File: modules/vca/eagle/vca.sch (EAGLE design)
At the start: 73 parts, among them IC1 TL074P, IC2 LM13600AN, Q1 2N3906, Q2 2N3906, T1 2N3904, T2 2N3904

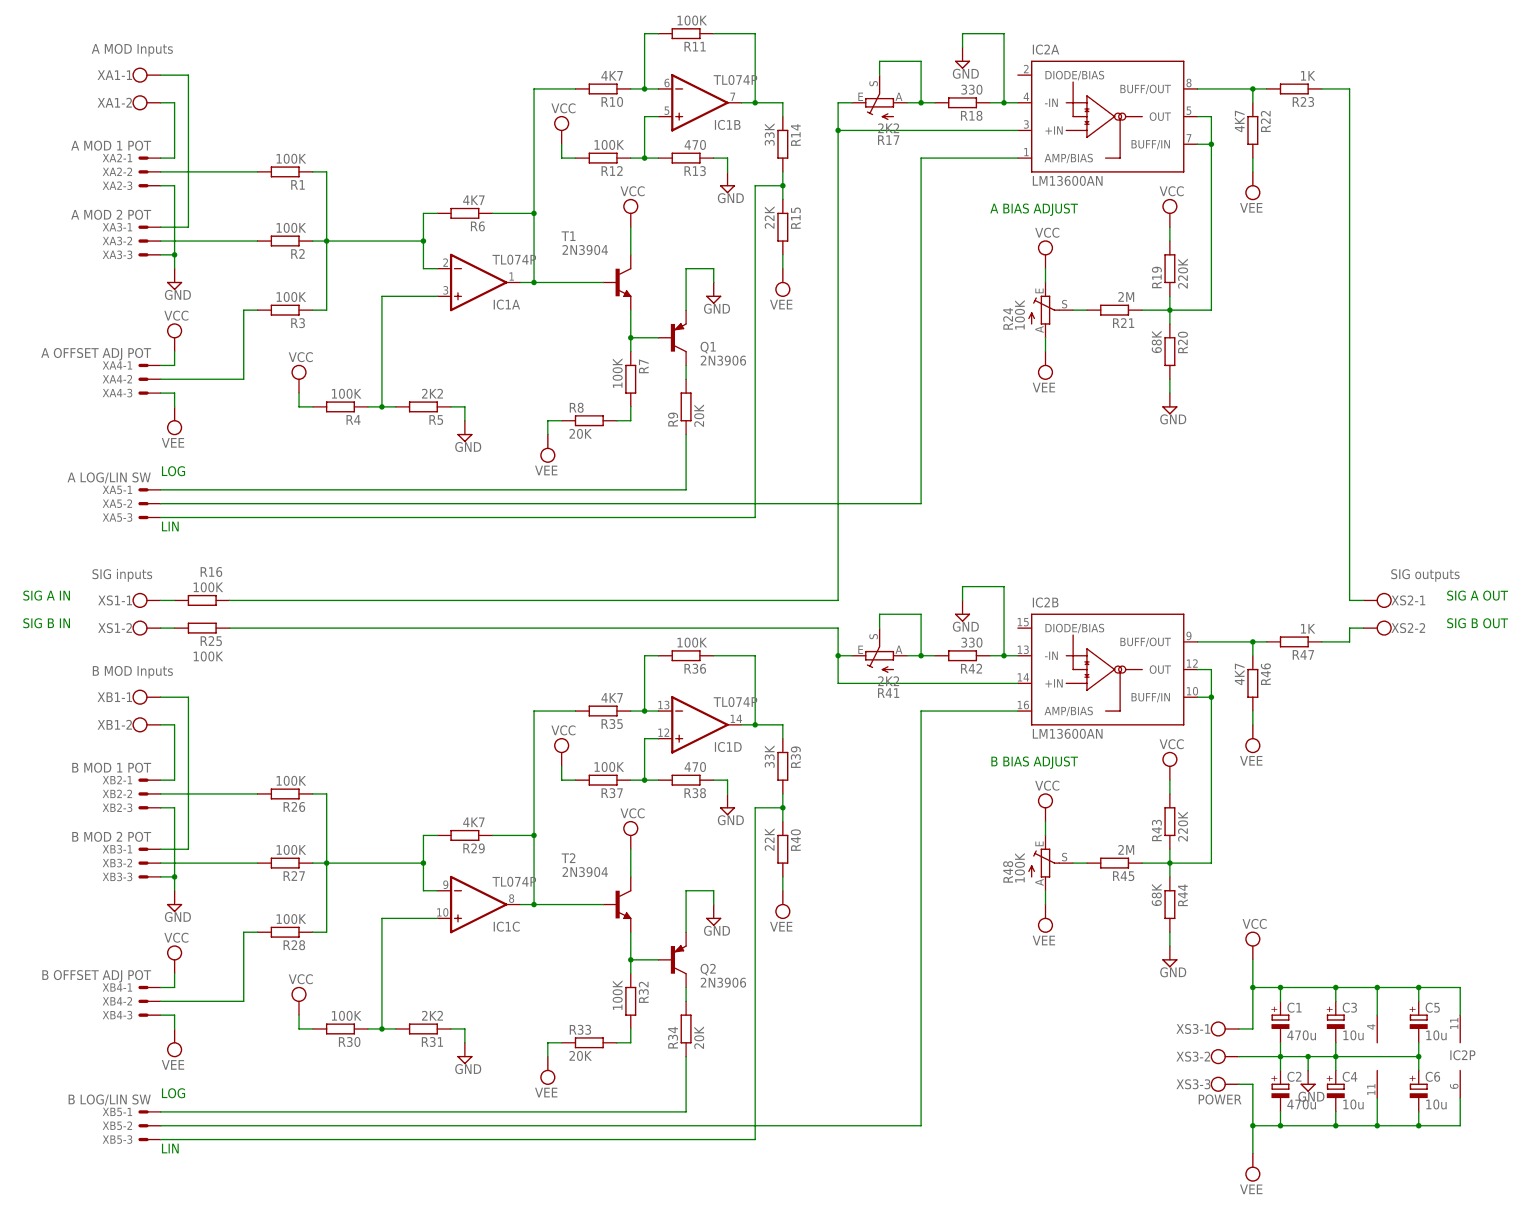
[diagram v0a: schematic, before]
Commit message: Basic layout of VCA board, still needs power
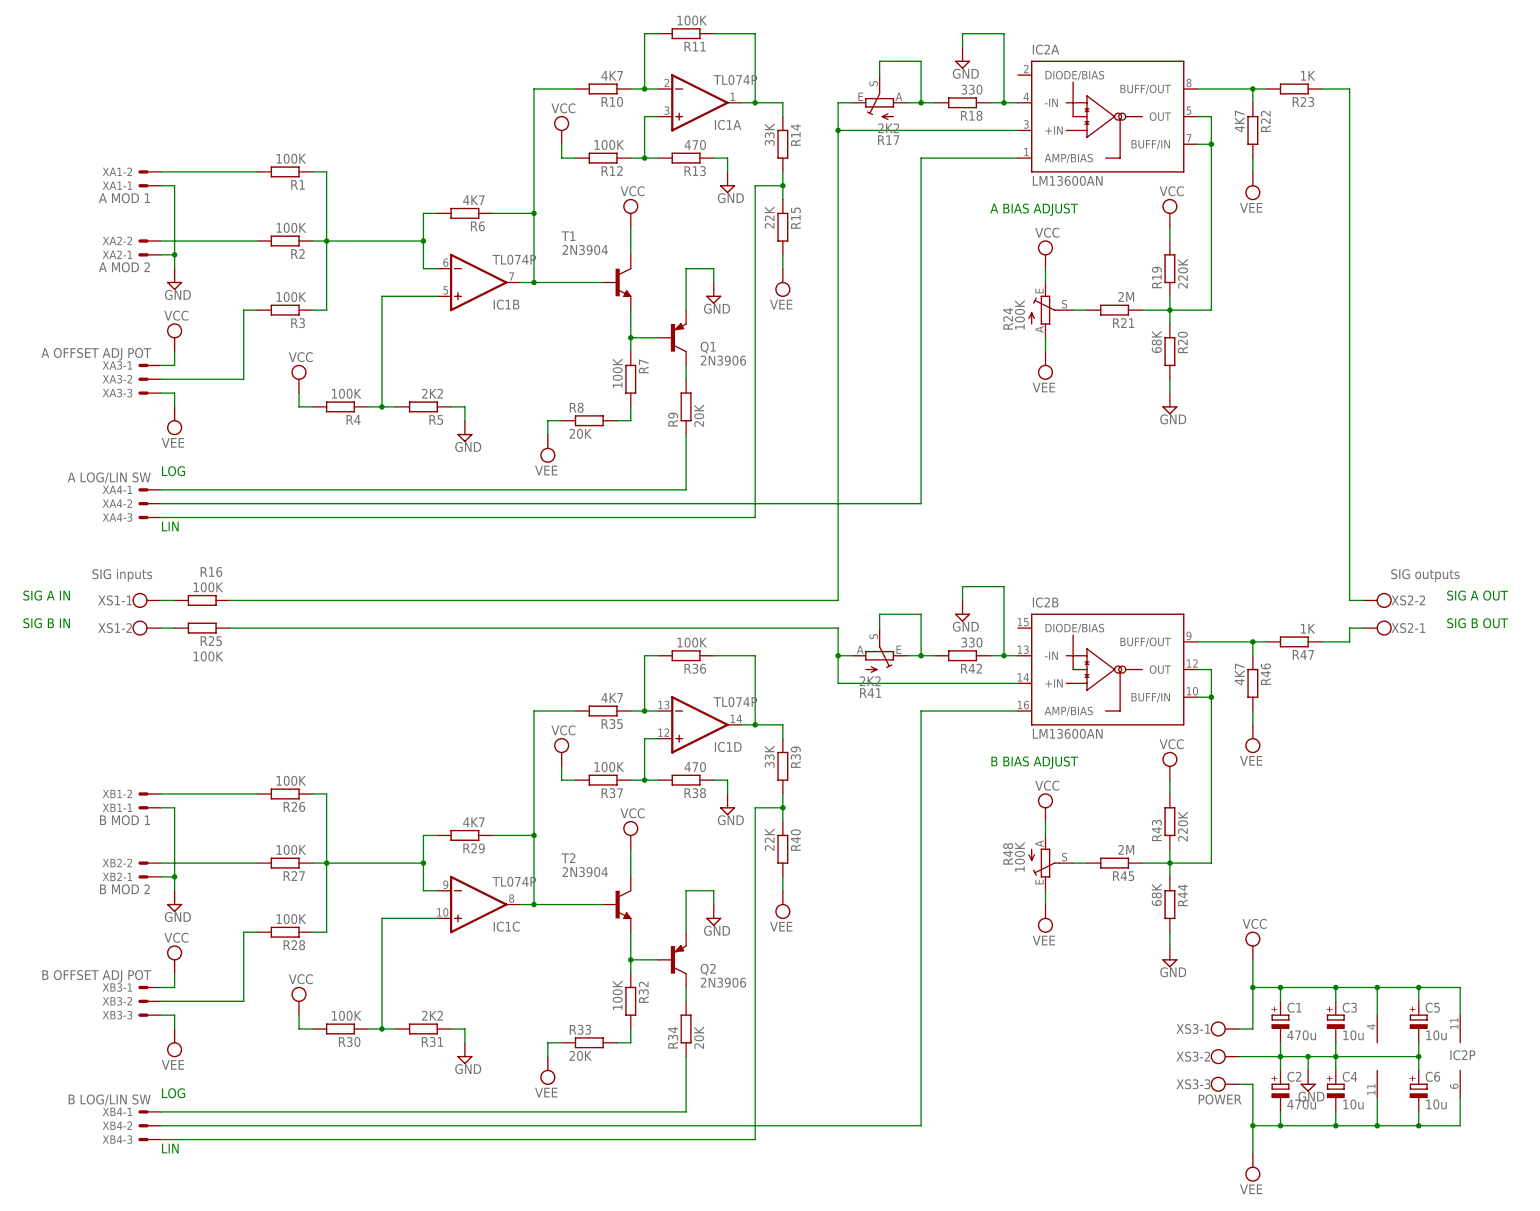
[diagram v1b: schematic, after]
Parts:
- removed XA5: A LOG/LIN SW, con-molex:22-23-2031
- removed XB5: B LOG/LIN SW, con-molex:22-23-2031
- XA1: value A MOD Inputs -> A MOD 1; device con-wago-500:W237-102 -> con-molex:22-23-2021
- XA2: value A MOD 1 POT -> A MOD 2; device con-molex:22-23-2031 -> con-molex:22-23-2021
- XA3: value A MOD 2 POT -> A OFFSET ADJ POT
- XA4: value A OFFSET ADJ POT -> A LOG/LIN SW
- XB1: value B MOD Inputs -> B MOD 1; device con-wago-500:W237-102 -> con-molex:22-23-2021
- XB2: value B MOD 1 POT -> B MOD 2; device con-molex:22-23-2031 -> con-molex:22-23-2021
- XB3: value B MOD 2 POT -> B OFFSET ADJ POT
- XB4: value B OFFSET ADJ POT -> B LOG/LIN SW
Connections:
- removed net N$19: XA1-1.KL, XA3-1.S
- removed net N$22: XA1-2.KL, XA2-1.S
- removed net N$33: XB1-2.KL, XB2-1.S
- removed net N$34: XB1-1.KL, XB3-1.S
- net GND: now also XA1-1.S, XA2-1.S, XB1-1.S, XB2-1.S; no longer XA2-3.S, XA3-3.S, XB2-3.S, XB3-3.S
- net N$1: now also IC1B.-IN; no longer IC1A.-IN
- net N$10: now also XA4-1.S; no longer XA5-1.S
- net N$11: now also IC1A.-IN; no longer IC1B.-IN
- net N$12: now also XA4-2.S; no longer XA5-2.S
- net N$13: now also IC1A.OUT; no longer IC1B.OUT
- net N$15: now also IC1A.+IN; no longer IC1B.+IN
- net N$17: now also XA4-3.S; no longer XA5-3.S
- net N$2: now also XA1-2.S; no longer XA2-2.S
- net N$25: now also R41.A; no longer R41.E
- net N$26: now also XB1-2.S; no longer XB2-2.S
- net N$27: now also XS2-2.KL; no longer XS2-1.KL
- net N$28: now also XB2-2.S; no longer XB3-2.S
- net N$29: now also XB3-2.S; no longer XB4-2.S
- net N$3: now also XA2-2.S; no longer XA3-2.S
- net N$30: now also XB4-1.S; no longer XB5-1.S
- net N$31: now also XS2-1.KL; no longer XS2-2.KL
- net N$32: now also XB4-2.S; no longer XB5-2.S
- net N$4: now also XA3-2.S; no longer XA4-2.S
- net N$45: now also XB4-3.S; no longer XB5-3.S
- net N$46: now also R41.E; no longer R41.A
- net N$5: now also IC1B.+IN; no longer IC1A.+IN
- net N$7: now also IC1B.OUT; no longer IC1A.OUT
- net VCC: now also R48.A, XA3-1.S, XB3-1.S; no longer R48.E, XA4-1.S, XB4-1.S
- net VEE: now also R48.E, XA3-3.S, XB3-3.S; no longer R48.A, XA4-3.S, XB4-3.S
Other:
- moved on the sheet: IC1A, IC1B, R48, XA1-1, XA1-2, XA2-1, XA2-2, XA3-1, XA3-2, XA3-3, XA4-1, XA4-2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

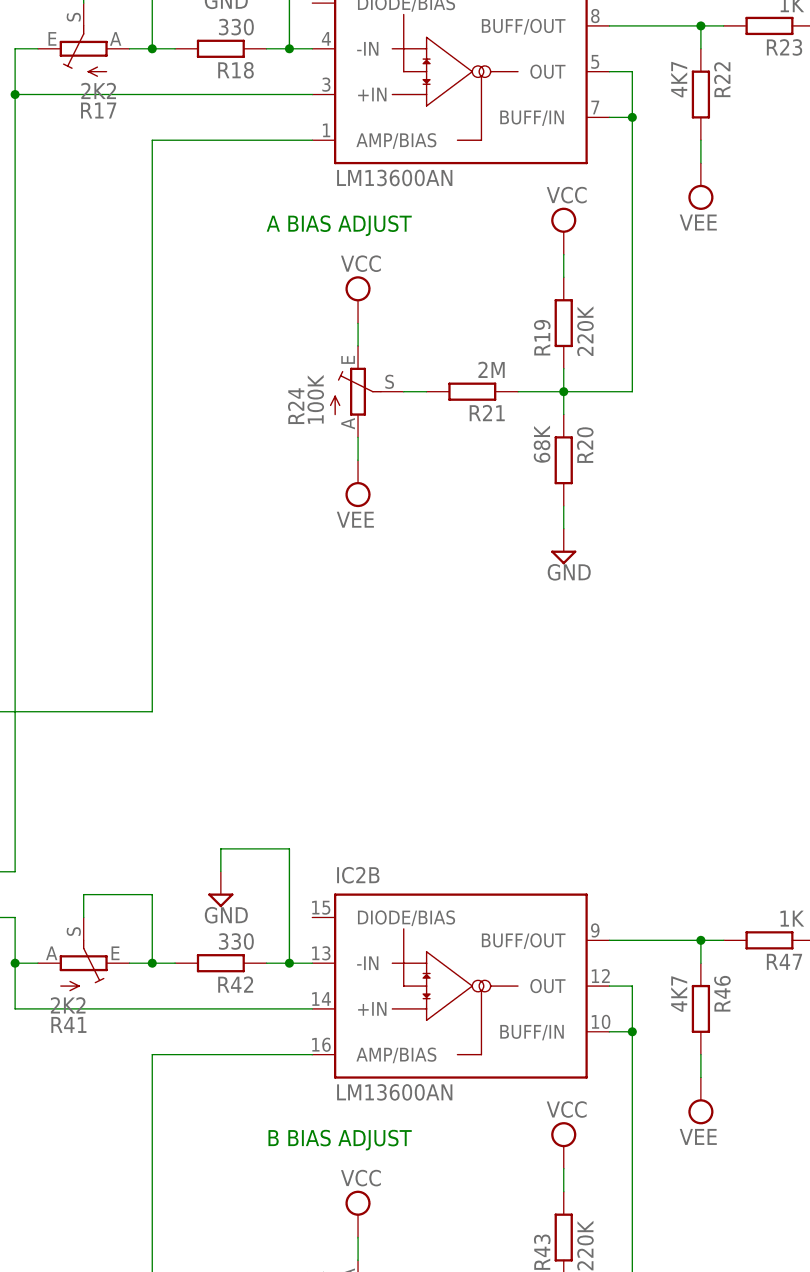
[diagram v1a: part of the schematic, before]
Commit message: Finish dual VCA board design
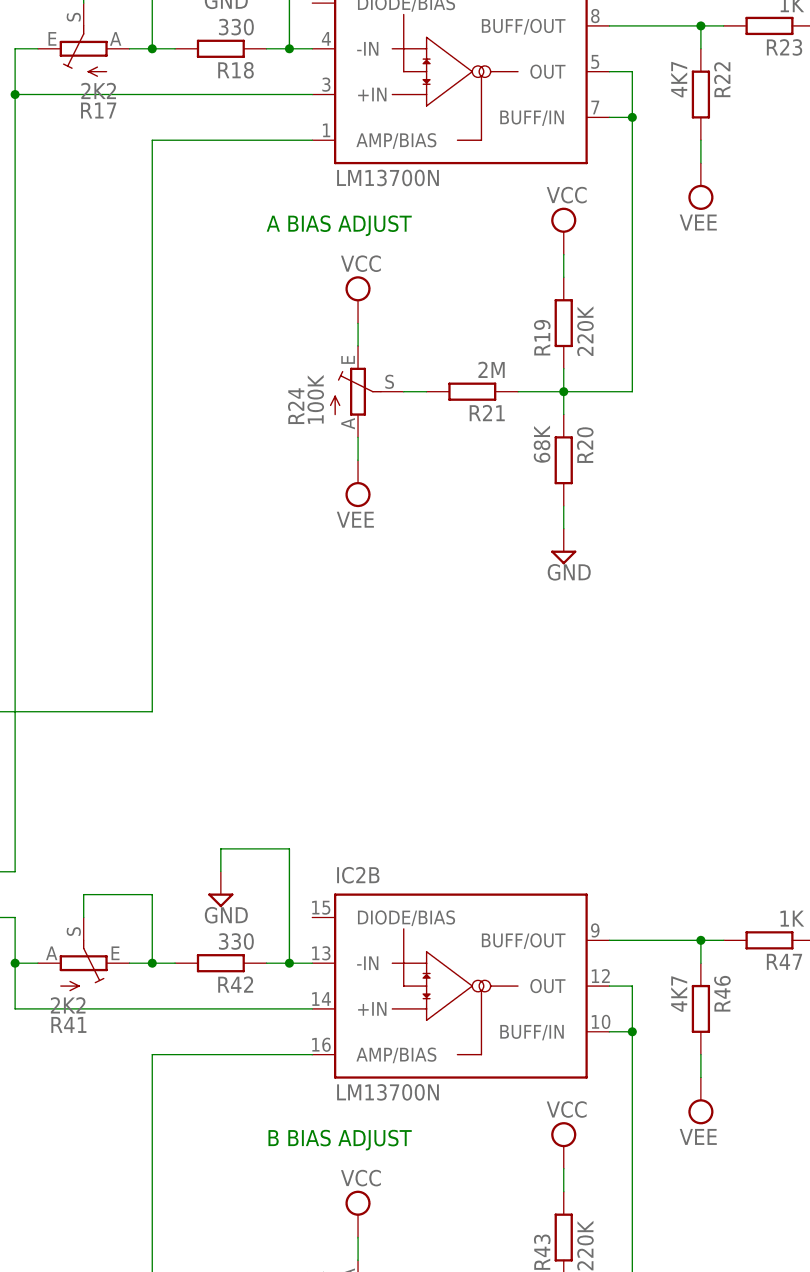
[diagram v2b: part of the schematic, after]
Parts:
- IC2: value LM13600AN -> LM13700N
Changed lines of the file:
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@@
 <parts>
 <part name="IC1" library="linear" deviceset="TL074" device="P"/>
-<part name="IC2" library="national-semiconductor" deviceset="LM13600" device="N" technology="A"/>
+<part name="IC2" library="national-semiconductor" deviceset="LM13600" device="N" technology="A" value="LM13700N"/>
 <part name="R1" library="rcl" deviceset="R-EU_" device="0204/7" value="100K"/>
 <part name="R2" library="rcl" deviceset="R-EU_" device="0204/7" value="100K"/>
